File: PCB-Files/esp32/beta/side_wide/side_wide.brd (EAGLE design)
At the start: 50 x 31 mm, 9 parts

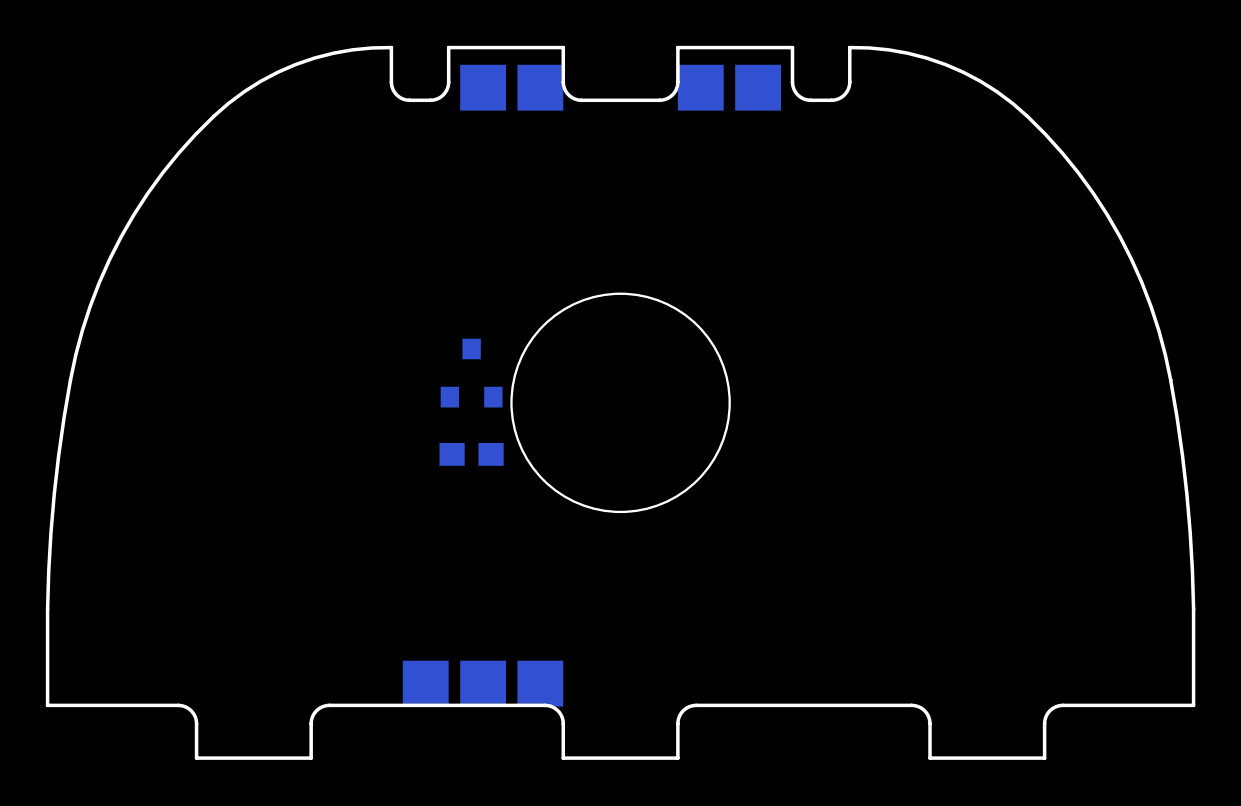
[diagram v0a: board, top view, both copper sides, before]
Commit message: creates final PCB version; revised beta side pcbs to match beta main pcb pinouts
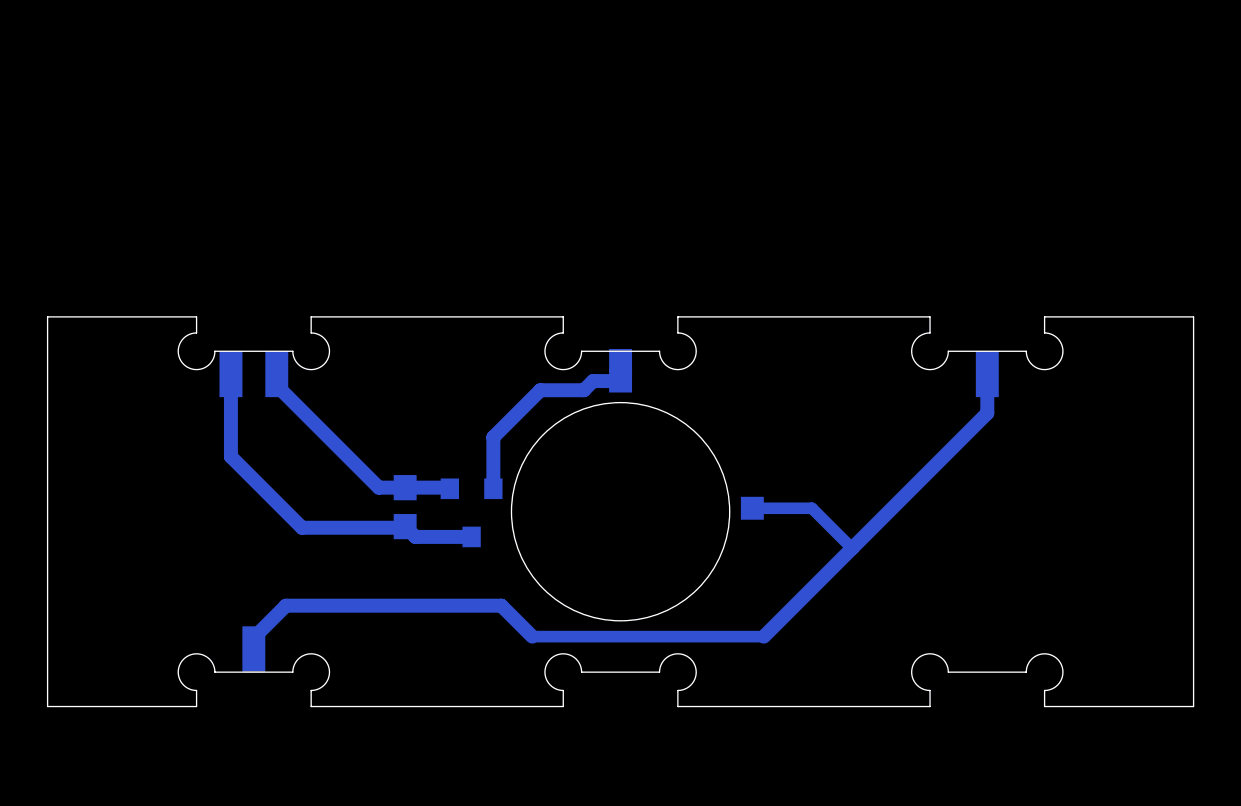
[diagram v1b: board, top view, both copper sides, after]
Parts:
- removed HALL_1_IN, HALL_1_OUT, HALL_2_IN, HALL_GND, HALL_GND1, HALL_VCC, HALL_VCC1: TPTP20SQ, testpad:TP20SQ
- added TP1, TP10, TP11, TP2, TP3, TP4, TP5, TP6, TP7, TP8, TP9: TPTP10SQ, testpad:TP10SQ
- moved HALL 6.00 mm to (18.5, 8.50), turned to 180 degrees
- moved C3 3.70 mm to (15.6, 8.70), turned to 90 degrees
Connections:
- removed net HALL_2: HALL.2, HALL_2_IN.TP
- new net TOUCH: TP10.TP, TP11.TP, TP7.TP, TP8.TP, TP9.TP
- net GND: now also TP3.TP, TP6.TP; no longer HALL_GND.TP, HALL_GND1.TP
- net HALL_1: now also HALL.2, TP2.TP, TP5.TP; no longer HALL_1_IN.TP, HALL_1_OUT.TP
- net VCC: now also TP1.TP, TP4.TP; no longer HALL_VCC.TP, HALL_VCC1.TP
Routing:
- net TOUCH: track 0.00 -> 45.5 mm
- net GND: track 0.00 -> 16.1 mm
- net VCC: track 0.00 -> 10.4 mm
- net HALL_1: track 0.00 -> 9.71 mm
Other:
- board size 50 x 31 mm -> 50 x 17 mm
